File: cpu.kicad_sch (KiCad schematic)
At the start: 26 parts, among them U1 68000D, U10 74LS244, U11 74LS373, U12 74LS244, U13 74LS373, U2 FAT_AGNUS_8375, U33 74LS258, U37 74LS32, U5 GARY_5719, X1 XTAL

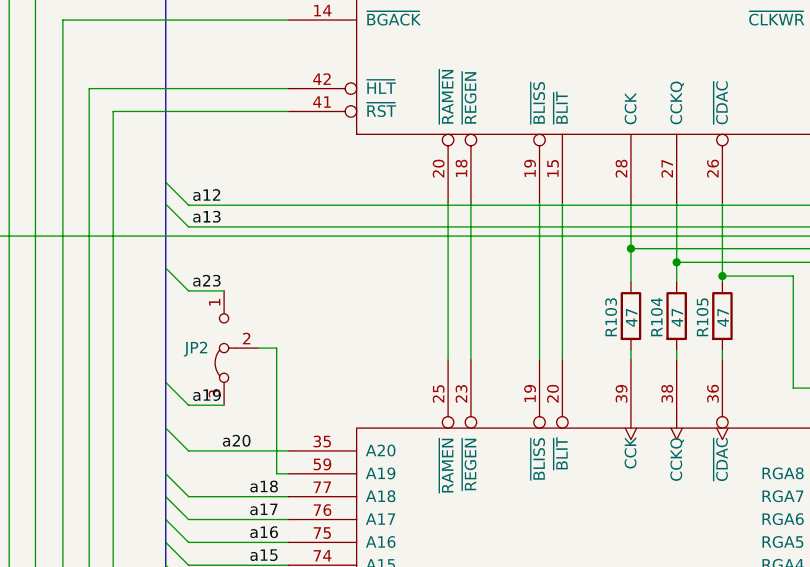
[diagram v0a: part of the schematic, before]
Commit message: DRAM chips replaced with SIMM module
Added logic to decode 2MB chip + 1.5MB slow
Rewired trapdoor slot
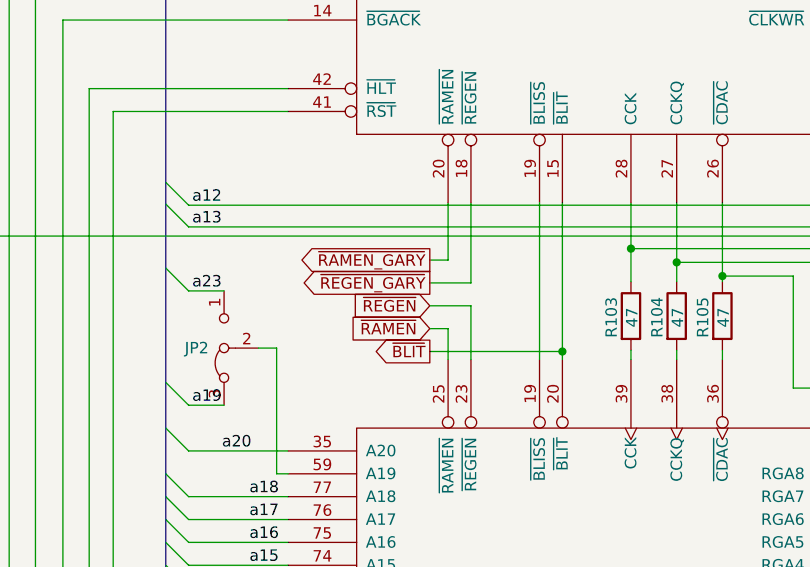
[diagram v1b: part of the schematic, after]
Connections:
- net ~{BLIT}: now reaches U2.20 (~{BLIT}), U5.15 (~{BLIT})
- net ~{REGEN_GARY}: now reaches U5.18 (~{REGEN})
- net ~{REGEN_GARY}: no longer U2.23 (~{REGEN})
- net ~{RAMEN_GARY}: now reaches U5.20 (~{RAMEN})
- net ~{RAMEN_GARY}: no longer U2.25 (~{RAMEN})
- new net ~{RAMEN}: U2.25 (~{RAMEN})
- new net ~{REGEN}: U2.23 (~{REGEN})
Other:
- title: Rämixx500 -> Rämixx500_max
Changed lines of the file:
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@@
 	(paper "A3")
 	(title_block
-		(title "Rämixx500")
-		(date "2019-04-11")
-		(rev "1")
+		(title "Rämixx500_max")
+		(date "2026-03-13")
+		(rev "2")
 		(company "SukkoPera")
 		(comment 1 "PROCESSOR AND OTHER USEFUL COMPONENTS")
@@
 	)
 	(junction
+		(at 289.052 124.46)
+		(diameter 0)
+		(color 0 0 0 0)
+	)
+	(junction
 		(at 227.584 239.649)
 		(diameter 0)
@@
 	(wire
 		(pts
+			(xy 274.32 114.3) (xy 276.352 114.3)
+		)
+		(stroke
+			(width 0)
+			(type default)
+		)
+	)
+	(wire
+		(pts
 			(xy 66.929 135.509) (xy 61.976 135.509)
 		)
@@
 		)
 	)
+	(wire
+		(pts
+			(xy 278.892 125.349) (xy 278.892 119.38)
+		)
+		(stroke
+			(width 0)
+			(type default)
+		)
+	)
 	(bus
 		(pts
@@
 		)
 	)
+	(wire
+		(pts
+			(xy 276.352 125.349) (xy 276.352 121.92)
+		)
+		(stroke
+			(width 0)
+			(type default)
+		)
+	)
 	(bus
 		(pts
@@
 	(wire
 		(pts
+			(xy 278.892 107.95) (xy 278.892 116.84)
+		)
+		(stroke
+			(width 0)
+			(type default)
+		)
+	)
+	(wire
+		(pts
 			(xy 117.729 145.669) (xy 139.954 145.669)
 		)
@@
 		)
 	)
+	(wire
+		(pts
+			(xy 289.052 124.46) (xy 289.052 125.349)
+		)
+		(stroke
+			(width 0)
+			(type default)
+		)
+	)
 	(polyline
 		(pts
@@
 		)
 	)
-	(wire
-		(pts
-			(xy 276.352 125.349) (xy 276.352 107.95)
-		)
-		(stroke
-			(width 0)
-			(type default)
-		)
-	)
 	(bus
 		(pts
@@
 	(wire
 		(pts
-			(xy 278.892 107.95) (xy 278.892 125.349)
+			(xy 274.32 121.92) (xy 276.352 121.92)
 		)
 		(stroke
@@
 	(wire
 		(pts
+			(xy 274.32 116.84) (xy 278.892 116.84)
+		)
+		(stroke
+			(width 0)
+			(type default)
+		)
+	)
+	(wire
+		(pts
 			(xy 224.155 71.12) (xy 224.155 237.109)
 		)
@@
 	(wire
 		(pts
-			(xy 289.052 107.95) (xy 289.052 125.349)
+			(xy 289.052 107.95) (xy 289.052 124.46)
 		)
 		(stroke
@@
 	(wire
 		(pts
+			(xy 274.32 119.38) (xy 278.892 119.38)
+		)
+		(stroke
+			(width 0)
+			(type default)
+		)
+	)
+	(wire
+		(pts
 			(xy 227.584 73.66) (xy 258.572 73.66)
 		)
@@
 		)
 	)
+	(wire
+		(pts
+			(xy 276.352 107.95) (xy 276.352 114.3)
+		)
+		(stroke
+			(width 0)
+			(type default)
+		)
+	)
 	(bus
 		(pts
@@
 		)
 	)
+	(wire
+		(pts
+			(xy 274.32 124.46) (xy 289.052 124.46)
+		)
+		(stroke
+			(width 0)
+			(type default)
+		)
+	)
 	(bus
 		(pts
@@
 		)
 	)
+	(global_label "~{BLIT}"
+		(shape output)
+		(at 274.32 124.46 180)
+		(fields_autoplaced yes)
+		(effects
+			(font
+				(size 1.27 1.27)
+			)
+			(justify right)
+		)
+		(property "Intersheetrefs" "${INTERSHEET_REFS}"
+			(at 268.1185 124.46 0)
+			(effects
+				(font
+					(size 1.27 1.27)
+				)
+				(justify right)
+				(hide yes)
+			)
+		)
+	)
 	(global_label "~{DTACK}"
 		(shape input)
@@
 		)
 	)
+	(global_label "~{REGEN_GARY}"
+		(shape output)
+		(at 274.32 116.84 180)
+		(fields_autoplaced yes)
+		(effects
+			(font
+				(size 1.27 1.27)
+			)
+			(justify right)
+		)
+		(property "Intersheetrefs" "${INTERSHEET_REFS}"
+			(at 260.1357 116.84 0)
+			(effects
+				(font
+					(size 1.27 1.27)
+				)
+				(justify right)
+				(hide yes)
+			)
+		)
+	)
 	(global_label "~{BEER}"
 		(shape input)
@@
 		)
 	)
+	(global_label "~{RAMEN_GARY}"
+		(shape output)
+		(at 274.32 114.3 180)
+		(fields_autoplaced yes)
+		(effects
+			(font
+				(size 1.27 1.27)
+			)
+			(justify right)
+		)
+		(property "Intersheetrefs" "${INTERSHEET_REFS}"
+			(at 260.0147 114.3 0)
+			(effects
+				(font
+					(size 1.27 1.27)
+				)
+				(justify right)
+				(hide yes)
+			)
+		)
+	)
 	(global_label "~{VSYNC}"
 		(shape bidirectional)
@@
 		)
 	)
+	(global_label "~{RAMEN}"
+		(shape input)
+		(at 274.32 121.92 180)
+		(fields_autoplaced yes)
+		(effects
+			(font
+				(size 1.27 1.27)
+			)
+			(justify right)
+		)
+		(property "Intersheetrefs" "${INTERSHEET_REFS}"
+			(at 265.6995 121.92 0)
+			(effects
+				(font
+					(size 1.27 1.27)
+				)
+				(justify right)
+				(hide yes)
+			)
+		)
+	)
 	(global_label "~{UDS}"
 		(shape bidirectional)
@@
 				(hide yes)
 			)
+		)
+	)
+	(global_label "~{REGEN}"
+		(shape input)
+		(at 274.32 119.38 180)
+		(fields_autoplaced yes)
+		(effects
+			(font
+				(size 1.27 1.27)
+			)
+			(justify right)
+		)
+		(property "Intersheetrefs" "${INTERSHEET_REFS}"
+			(at 265.8205 119.38 0)
+			(effects
+				(font
+					(size 1.27 1.27)
+				)
+				(justify right)
+				(hide yes)
+			)

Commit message: removed JP2
some more small fixes
schematic is now more or less done I think
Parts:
- removed JP2: Jumper_3_Bridged23, Raemixx500:Jumper3-Bridged23, symbol Jumper_3_Bridged23:Jumper_3_Bridged23
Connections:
- net a19: now also U2.59 (A19)
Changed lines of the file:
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@@
 	)
 	(bus_entry
-		(at 244.983 115.189)
-		(size 2.54 2.54)
-		(stroke
-			(width 0)
-			(type default)
-		)
-	)
-	(bus_entry
 		(at 203.454 145.542)
 		(size 2.54 2.54)
@@
 	)
 	(bus_entry
-		(at 244.983 127.889)
+		(at 244.983 135.509)
 		(size 2.54 2.54)
 		(stroke
@@
 		)
 	)
-	(wire
-		(pts
-			(xy 255.27 124.079) (xy 257.302 124.079)
-		)
-		(stroke
-			(width 0)
-			(type default)
-		)
-	)
 	(bus
 		(pts
@@
 	(wire
 		(pts
-			(xy 257.302 124.079) (xy 257.302 138.049)
-		)
-		(stroke
-			(width 0)
-			(type default)
-		)
-	)
-	(wire
-		(pts
 			(xy 339.852 71.12) (xy 351.155 71.12)
 		)
@@
 	(wire
 		(pts
-			(xy 247.523 130.429) (xy 251.46 130.429)
-		)
-		(stroke
-			(width 0)
-			(type default)
-		)
-	)
-	(wire
-		(pts
 			(xy 184.785 94.869) (xy 203.454 94.869)
 		)
@@
 		)
 	)
-	(bus
-		(pts
-			(xy 244.983 132.969) (xy 244.983 138.049)
-		)
-		(stroke
-			(width 0)
-			(type default)
-		)
-	)
 	(wire
 		(pts
@@
 	(wire
 		(pts
-			(xy 257.302 138.049) (xy 258.572 138.049)
+			(xy 247.523 138.049) (xy 258.572 138.049)
 		)
 		(stroke
@@
 		)
 	)
-	(wire
-		(pts
-			(xy 258.572 135.509) (xy 247.523 135.509)
-		)
-		(stroke
-			(width 0)
-			(type default)
-		)
-	)
 	(bus
 		(pts
@@
 	(bus
 		(pts
-			(xy 244.983 115.189) (xy 244.983 127.889)
+			(xy 244.983 108.077) (xy 244.983 132.969)
 		)
 		(stroke
@@
 		)
 	)
+	(bus
+		(pts
+			(xy 244.983 135.509) (xy 244.983 138.049)
+		)
+		(stroke
+			(width 0)
+			(type default)
+		)
+	)
 	(wire
 		(pts
@@
 	(wire
 		(pts
+			(xy 247.523 135.509) (xy 258.572 135.509)
+		)
+		(stroke
+			(width 0)
+			(type default)
+		)
+	)
+	(wire
+		(pts
 			(xy 258.572 204.089) (xy 247.523 204.089)
 		)
@@
 	(wire
 		(pts
-			(xy 247.523 117.729) (xy 251.46 117.729)
-		)
-		(stroke
-			(width 0)
-			(type default)
-		)
-	)
-	(wire
-		(pts
 			(xy 196.596 263.144) (xy 196.596 265.43)
 		)
@@
 	(bus
 		(pts
-			(xy 244.983 108.077) (xy 244.983 115.189)
-		)
-		(stroke
-			(width 0)
-			(type default)
-		)
-	)
-	(bus
-		(pts
 			(xy 244.983 193.929) (xy 244.983 196.469)
 		)
@@
 	(bus
 		(pts
+			(xy 244.983 132.969) (xy 244.983 135.509)
+		)
+		(stroke
+			(width 0)
+			(type default)
+		)
+	)
+	(bus
+		(pts
 			(xy 142.494 135.509) (xy 142.494 137.922)
 		)
@@
 		)
 	)
-	(bus
-		(pts
-			(xy 244.983 127.889) (xy 244.983 132.969)
-		)
-		(stroke
-			(width 0)
-			(type default)
-		)
-	)
 	(wire
 		(pts
@@
 	)
 	(label "a19"
-		(at 251.206 130.429 180)
+		(at 257.556 138.049 180)
 		(effects
 			(font
@@
 		)
 	)
-	(label "a23"
-		(at 251.206 117.729 180)
-		(effects
-			(font
-				(size 1.27 1.27)
-			)
-			(justify right bottom)
-		)
-	)
 	(label "drd6"
 		(at 257.556 211.709 180)
@@
 	)
 	(label "a20"
-		(at 254.508 135.509 180)
+		(at 257.556 135.509 180)
 		(effects
 			(font
@@
 				)
 			)
-		)
-	)
-	(symbol
-		(lib_id "Jumper_3_Bridged23:Jumper_3_Bridged23")
-		(at 251.46 124.079 90)
-		(mirror x)
-		(unit 1)
-		(exclude_from_sim no)
-		(in_bom yes)
-		(on_board yes)
-		(dnp no)
-		(property "Reference" "JP2"
-			(at 249.7582 124.079 90)
-			(effects
-				(font
-					(size 1.27 1.27)
-				)
-				(justify left)
-			)
-		)
-		(property "Value" "Jumper_3_Bridged23"
-			(at 249.7836 122.936 90)
-			(effects
-				(font
-					(size 1.27 1.27)
-				)
-				(justify left)
-				(hide yes)
-			)
-		)
-		(property "Footprint" "Raemixx500:Jumper3-Bridged23"
-			(at 251.46 124.079 0)
-			(effects
-				(font
-					(size 1.27 1.27)
-				)
-				(hide yes)
-			)
-		)
-		(property "Datasheet" "~"
-			(at 251.46 124.079 0)
-			(effects
-				(font
-					(size 1.27 1.27)
-				)
-				(hide yes)
-			)
-		)
-		(property "Description" ""
-			(at 251.46 124.079 0)
-			(effects
-				(font
-					(size 1.27 1.27)
-				)
-			)
-		)
-		(property "MFG Name" "SKIP"
-			(at 251.46 124.079 0)
-			(effects
-				(font
-					(size 1.27 1.27)
-				)
-				(hide yes)
-			)
-		)
-		(property "MFG Part Num" "SKIP"
-			(at 251.46 124.079 0)
-			(effects
-				(font
-					(size 1.27 1.27)
-				)
-				(hide yes)
-			)
-		)
-		(property "Section" "JMP"
-			(at 251.46 124.079 0)
-			(effects
-				(font
-					(size 1.27 1.27)
-				)
-				(hide yes)
-			)
-		)
-		(pin "3"
-		)
-		(pin "1"
-		)
-		(pin "2"
-		)
-		(instances
-			(project "Raemixx500"
-				(path "/a9c87613-fb8b-4be0-8e87-0d76f8b56421/00000000-0000-0000-0000-00005cae5331"
-					(reference "JP2")
-					(unit 1)
-				)
-			)

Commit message: Working on BOM
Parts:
- C99: MFG Name AVX -> VISHAY; MFG Part Num SA115C104KAR -> A104K15X7RF5TAA; Mouser (none) -> 594-A104K15X7RF5TAA
- E666: MFG Name AVX -> KEMET; MFG Part Num SA102A220JARC -> C410C220J1G5TA; Mouser (none) -> 80-C410C220J1G

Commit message: more work on BOM done
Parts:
- FB101, R111, R112, R114: MFG Name (none) -> YAGEO; MFG Part Num (none) -> MFR-25FBF52-68R; Mouser (none) -> 603-MFR-25FBF52-68R
- FB102: MFG Name (none) -> YAGEO; MFG Part Num (none) -> MFR-25FBF52-150R; Mouser (none) -> 603-MFR-25FBF52-150R
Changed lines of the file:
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@@
 			)
 		)
-		(property "Mouser" ""
+		(property "Mouser" "603-MFR-25FBF52-68R "
+			(at 336.042 71.12 90)
+			(effects
+				(font
+					(size 1.27 1.27)
+				)
+				(hide yes)
+			)
+		)
+		(property "MFG Name" "YAGEO"
+			(at 336.042 71.12 90)
+			(effects
+				(font
+					(size 1.27 1.27)
+				)
+				(hide yes)
+			)
+		)
+		(property "MFG Part Num" "MFR-25FBF52-68R "
 			(at 336.042 71.12 90)
 			(effects
@@
 			)
 		)
-		(property "Mouser" ""
+		(property "Mouser" "603-MFR-25FBF52-68R "
+			(at 235.458 29.21 90)
+			(effects
+				(font
+					(size 1.27 1.27)
+				)
+				(hide yes)
+			)
+		)
+		(property "MFG Name" "YAGEO"
+			(at 235.458 29.21 90)
+			(effects
+				(font
+					(size 1.27 1.27)
+				)
+				(hide yes)
+			)
+		)
+		(property "MFG Part Num" "MFR-25FBF52-68R "
 			(at 235.458 29.21 90)
 			(effects
@@
 			)
 		)
-		(property "Mouser" ""
+		(property "Mouser" "603-MFR-25FBF52-68R "
+			(at 235.458 31.75 90)
+			(effects
+				(font
+					(size 1.27 1.27)
+				)
+				(hide yes)
+			)
+		)
+		(property "MFG Name" "YAGEO"
+			(at 235.458 31.75 90)
+			(effects
+				(font
+					(size 1.27 1.27)
+				)
+				(hide yes)
+			)
+		)
+		(property "MFG Part Num" "MFR-25FBF52-68R "
 			(at 235.458 31.75 90)
 			(effects
@@
 			)
 		)
-		(property "Mouser" ""
+		(property "Mouser" "603-MFR-25FBF52-68R "
+			(at 196.596 260.604 0)
+			(effects
+				(font
+					(size 1.27 1.27)
+				)
+				(hide yes)
+			)
+		)
+		(property "MFG Name" "YAGEO"
+			(at 196.596 260.604 0)
+			(effects
+				(font
+					(size 1.27 1.27)
+				)
+				(hide yes)
+			)
+		)
+		(property "MFG Part Num" "MFR-25FBF52-68R "
 			(at 196.596 260.604 0)
 			(effects
@@
 			)
 		)
-		(property "Mouser" ""
+		(property "Mouser" "603-MFR-25FBF52-150R"
+			(at 238.633 263.144 0)
+			(effects
+				(font
+					(size 1.27 1.27)
+				)
+				(hide yes)
+			)
+		)
+		(property "MFG Name" "YAGEO"
+			(at 238.633 263.144 0)
+			(effects
+				(font
+					(size 1.27 1.27)
+				)
+				(hide yes)
+			)
+		)
+		(property "MFG Part Num" "MFR-25FBF52-150R"
 			(at 238.633 263.144 0)
 			(effects

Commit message: More BOM work
I am marking optional components as DNP to get some overview
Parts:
- R101, R102: MFG Name (none) -> YAGEO; MFG Part Num (none) -> MFR-25FBF52-27R; Mouser (none) -> 603-MFR-25FBF52-27R
- R103, R104, R105, R106, R107, R113: MFG Name (none) -> YAGEO; MFG Part Num (none) -> MFR-25FBF52-47R; Mouser (none) -> 603-MFR-25FBF52-47R
- U1: MFG Name (none) -> MOTOROLA
- U2, U5: MFG Name (none) -> COMMODORE
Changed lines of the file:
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@@
 			)
 		)
+		(property "MFG Name" "COMMODORE"
+			(at 291.592 190.119 0)
+			(effects
+				(font
+					(size 1.27 1.27)
+				)
+				(hide yes)
+			)
+		)
 		(pin "35"
 		)
@@
 			)
 		)
-		(property "Mouser" ""
+		(property "Mouser" "603-MFR-25FBF52-47R "
+			(at 296.672 120.523 90)
+			(effects
+				(font
+					(size 1.27 1.27)
+				)
+				(hide yes)
+			)
+		)
+		(property "MFG Name" "YAGEO"
+			(at 296.672 120.523 90)
+			(effects
+				(font
+					(size 1.27 1.27)
+				)
+				(hide yes)
+			)
+		)
+		(property "MFG Part Num" "MFR-25FBF52-47R"
 			(at 296.672 120.523 90)
 			(effects
@@
 			)
 		)
-		(property "Mouser" ""
+		(property "Mouser" "603-MFR-25FBF52-47R "
+			(at 301.752 120.523 90)
+			(effects
+				(font
+					(size 1.27 1.27)
+				)
+				(hide yes)
+			)
+		)
+		(property "MFG Name" "YAGEO"
+			(at 301.752 120.523 90)
+			(effects
+				(font
+					(size 1.27 1.27)
+				)
+				(hide yes)
+			)
+		)
+		(property "MFG Part Num" "MFR-25FBF52-47R"
 			(at 301.752 120.523 90)
 			(effects
@@
 			)
 		)
-		(property "Mouser" ""
+		(property "Mouser" "603-MFR-25FBF52-47R "
+			(at 306.832 120.523 90)
+			(effects
+				(font
+					(size 1.27 1.27)
+				)
+				(hide yes)
+			)
+		)
+		(property "MFG Name" "YAGEO"
+			(at 306.832 120.523 90)
+			(effects
+				(font
+					(size 1.27 1.27)
+				)
+				(hide yes)
+			)
+		)
+		(property "MFG Part Num" "MFR-25FBF52-47R"
 			(at 306.832 120.523 90)
 			(effects
@@
 			)
 		)
-		(property "Mouser" ""
+		(property "Mouser" "603-MFR-25FBF52-47R "
+			(at 340.233 219.329 90)
+			(effects
+				(font
+					(size 1.27 1.27)
+				)
+				(hide yes)
+			)
+		)
+		(property "MFG Name" "YAGEO"
+			(at 340.233 219.329 90)
+			(effects
+				(font
+					(size 1.27 1.27)
+				)
+				(hide yes)
+			)
+		)
+		(property "MFG Part Num" "MFR-25FBF52-47R"
 			(at 340.233 219.329 90)
 			(effects
@@
 			)
 		)
-		(property "Mouser" ""
+		(property "Mouser" "603-MFR-25FBF52-47R "
+			(at 340.233 215.773 90)
+			(effects
+				(font
+					(size 1.27 1.27)
+				)
+				(hide yes)
+			)
+		)
+		(property "MFG Name" "YAGEO"
+			(at 340.233 215.773 90)
+			(effects
+				(font
+					(size 1.27 1.27)
+				)
+				(hide yes)
+			)
+		)
+		(property "MFG Part Num" "MFR-25FBF52-47R"
 			(at 340.233 215.773 90)
 			(effects
@@
 			)
 		)
-		(property "Mouser" ""
+		(property "Mouser" "603-MFR-25FBF52-27R "
+			(at 250.19 81.28 90)
+			(effects
+				(font
+					(size 1.27 1.27)
+				)
+				(hide yes)
+			)
+		)
+		(property "MFG Name" "YAGEO"
+			(at 250.19 81.28 90)
+			(effects
+				(font
+					(size 1.27 1.27)
+				)
+				(hide yes)
+			)
+		)
+		(property "MFG Part Num" "MFR-25FBF52-27R"
 			(at 250.19 81.28 90)
 			(effects
@@
 			)
 		)
-		(property "Mouser" ""
+		(property "Mouser" "603-MFR-25FBF52-27R "
+			(at 235.585 59.69 90)
+			(effects
+				(font
+					(size 1.27 1.27)
+				)
+				(hide yes)
+			)
+		)
+		(property "MFG Name" "YAGEO"
+			(at 235.585 59.69 90)
+			(effects
+				(font
+					(size 1.27 1.27)
+				)
+				(hide yes)
+			)
+		)
+		(property "MFG Part Num" "MFR-25FBF52-27R"
 			(at 235.585 59.69 90)
 			(effects
@@
 			)
 		)
+		(property "MFG Name" "MOTOROLA"
+			(at 92.329 117.729 0)
+			(effects
+				(font
+					(size 1.27 1.27)
+				)
+				(hide yes)
+			)
+		)
 		(pin "25"
 		)
@@
 			)
 		)
-		(property "Mouser" ""
+		(property "Mouser" "603-MFR-25FBF52-47R "
+			(at 235.458 26.67 90)
+			(effects
+				(font
+					(size 1.27 1.27)
+				)
+				(hide yes)
+			)
+		)
+		(property "MFG Name" "YAGEO"
+			(at 235.458 26.67 90)
+			(effects
+				(font
+					(size 1.27 1.27)
+				)
+				(hide yes)
+			)
+		)
+		(property "MFG Part Num" "MFR-25FBF52-47R"
 			(at 235.458 26.67 90)
 			(effects
@@
 			(at 291.592 62.23 0)
 			(effects
+				(font
+					(size 1.27 1.27)
+				)
+				(hide yes)
+			)
+		)
+		(property "MFG Name" "COMMODORE"
+			(at 291.592 62.23 0)
+			(effects
